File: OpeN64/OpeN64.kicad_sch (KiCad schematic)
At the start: 269 parts, among them P6 P5, SW1 N64_SW1_Power, SW2 RESET, U13 78M05, x1 Crystal_Small, x2 Crystal_Small

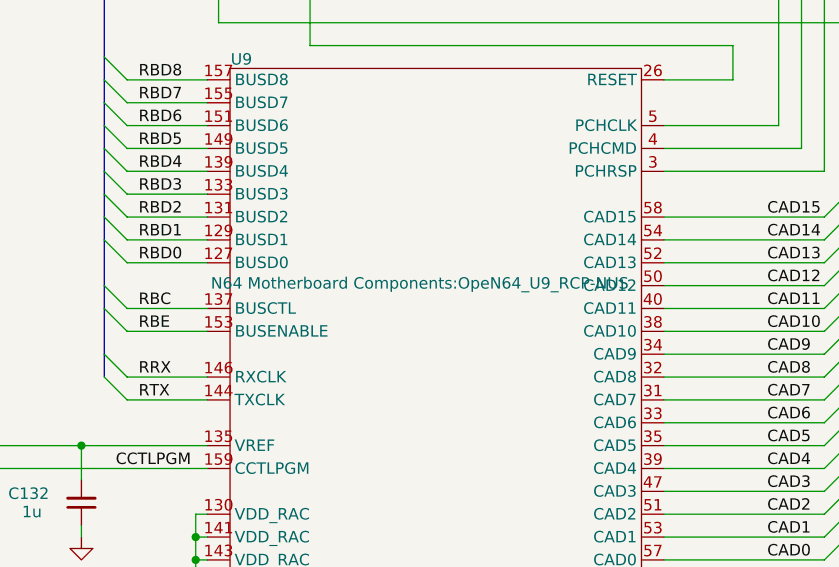
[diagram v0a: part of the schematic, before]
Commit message: Correct footprint associations after library rename
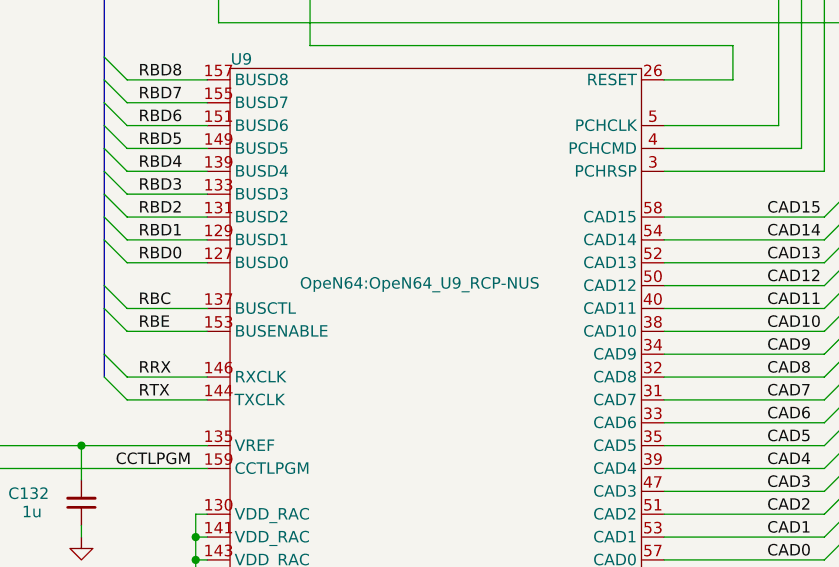
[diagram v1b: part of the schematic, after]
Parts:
- C1, C100, C101, C102, C103, C104, C105, C106, C107, C108, C109, C11, C110, C111, C113, C115, C116, C12, C120, C121, C122, C127, C129, C13, C136, C137, C139, C14, C143, C146, C147, C148, C150, C151, C152, C153, C154, C155, C156, C157, C158, C159, C160, C161, C162, C163, C164, C165, C166, C167, C168, C169, C17, C170, C172, C176, C177, C178, C179, C18, C19, C2, C20, C21, C22, C23, C27, C29, C3, C30, C31, C32, C35, C36, C38, C39, C4, C40, C41, C42, C45, C46, C47, C48, C49, C50, C51, C52, C54, C55, C56, C57, C58, C6, C64, C67, C68, C69, C7, C70, C71, C72, C75, C76, C77, C78, C8, C80, C83, C85, C86, C87, C88, C9, C90, C91, C93, C94, C96, C99, R1, R10, R11, R12, R13, R14, R15, R16, R17, R18, R19, R2, R20, R21, R22, R23, R28, R3, R31, R34, R36, R37, R38, R39, R4, R40, R5, R53, R54, R55, R56, R57, R58, R6, R7, R8, R9: footprint N64 Motherboard Components:OpeN64_SMD_0603 -> OpeN64:OpeN64_SMD_0603
- C10, C112, C114, C117, C118, C119, C123, C124, C125, C126, C132, C133, C135, C138, C144, C149, C37, C43, C44, C5, C53, C59, C60, C61, C62, C63, C65, C66, C74, C79, C82, C84, C89, C92, C95, C97, C98, R24, R25, R26, R27, R29, R30, R32, R33, R35: footprint N64 Motherboard Components:OpeN64_SMD_0805 -> OpeN64:OpeN64_SMD_0805
- C128, C34: footprint N64 Motherboard Components:OpeN64_CAP_AL_SMD_3.8x4.5 -> OpeN64:OpeN64_CAP_AL_SMD_3.8x4.5
- C130, C131, C134, C140, C141, C142, C145, C24, C28, C33, C73, C81: footprint N64 Motherboard Components:OpeN64_CAP_AL_SMD_6.2x4.7 -> OpeN64:OpeN64_CAP_AL_SMD_6.2x4.7
- C15, C16: footprint N64 Motherboard Components:OpeN64_CAP_AL_SMD_7.8x4.9 -> OpeN64:OpeN64_CAP_AL_SMD_7.8x4.9
- C173, C174, C175: footprint N64 Motherboard Components:OpeN64_SMD_1206 -> OpeN64:OpeN64_SMD_1206
- C25, C26: footprint N64 Motherboard Components:OpeN64_CAP_AL_SMD_3.8x4.5_Flipped -> OpeN64:OpeN64_CAP_AL_SMD_3.8x4.5_Flipped
- D1, D2: footprint N64 Motherboard Components:OpeN64_Diode -> OpeN64:OpeN64_Diode
- D3: footprint N64 Motherboard Components:OpeN64_D3_Red_LED -> OpeN64:OpeN64_D3_Red_LED
- D4, D5: footprint N64 Motherboard Components:OpeN64_Diode_Array_5_Pin -> OpeN64:OpeN64_Diode_Array_5_Pin
- DA1, DA3, DA5, DA6, DA7, DA8: footprint N64 Motherboard Components:OpeN64_Diode_Array -> OpeN64:OpeN64_Diode_Array
- FIL1, FIL2, FIL3, FIL4, FIL5, FIL6, FIL7, FIL8: footprint N64 Motherboard Components:OpeN64_Filter -> OpeN64:OpeN64_Filter
- P1: footprint N64 Motherboard Components:OpeN64_P1_RDRAM_Expansion_Port -> OpeN64:OpeN64_P1_RDRAM_Expansion_Port
- P2: footprint N64 Motherboard Components:OpeN64_P2_Left_Controller_Port -> OpeN64:OpeN64_P2_Left_Controller_Port
- P3: footprint N64 Motherboard Components:OpeN64_P3_Right_Controller_Port -> OpeN64:OpeN64_P3_Right_Controller_Port
- P4: footprint N64 Motherboard Components:OpeN64_P4_Power_Port -> OpeN64:OpeN64_P4_Power_Port
- P6: footprint N64 Motherboard Components:OpeN64_P5_Cartridge_Slot -> OpeN64:OpeN64_P5_Cartridge_Slot
- P7: footprint N64 Motherboard Components:OpeN64_P7_Video_Port -> OpeN64:OpeN64_P7_Video_Port
- Q1: footprint N64 Motherboard Components:OpeN64_Q_T23 -> OpeN64:OpeN64_Q_T23
- SW1: footprint N64 Motherboard Components:OpeN64_SW1_Power_Switch -> OpeN64:OpeN64_SW1_Power_Switch
- SW2: footprint N64 Motherboard Components:OpeN64_SW2_Reset -> OpeN64:OpeN64_SW2_Reset
- U1: footprint N64 Motherboard Components:OpeN64_U1_9480F -> OpeN64:OpeN64_U1_9480F
- U10: footprint N64 Motherboard Components:OpeN64_U10_CPU-NUS -> OpeN64:OpeN64_U10_CPU-NUS
- U11, U14: footprint N64 Motherboard Components:OpeN64_U11_14_RDRAM18-NUS -> OpeN64:OpeN64_U11_14_RDRAM18-NUS
- U12: footprint N64 Motherboard Components:OpeN64_U12_PQ7VZ5 -> OpeN64:OpeN64_U12_PQ7VZ5
- U13: footprint N64 Motherboard Components:OpeN64_U13_TO-252 -> OpeN64:OpeN64_U13_TO-252
- U15, U7: footprint N64 Motherboard Components:OpeN64_U7_15_MX8330 -> OpeN64:OpeN64_U7_15_MX8330
- U2: footprint N64 Motherboard Components:OpeN64_U2_AMP_NUS -> OpeN64:OpeN64_U2_AMP_NUS
- U3: footprint N64 Motherboard Components:OpeN64_U3_PST9128 -> OpeN64:OpeN64_U3_PST9128
- U4: footprint N64 Motherboard Components:OpeN64_U4_VDC-NUS -> OpeN64:OpeN64_U4_VDC-NUS
- U5: footprint N64 Motherboard Components:OpeN64_U5_ENC-NUS -> OpeN64:OpeN64_U5_ENC-NUS
- U6: footprint N64 Motherboard Components:OpeN64_U6_PIF -> OpeN64:OpeN64_U6_PIF
- U8: footprint N64 Motherboard Components:OpeN64_U8_LV125A -> OpeN64:OpeN64_U8_LV125A
- U9: footprint N64 Motherboard Components:OpeN64_U9_RCP-NUS -> OpeN64:OpeN64_U9_RCP-NUS
- x1, x2: footprint N64 Motherboard Components:OpeN64_CRYSTAL_HC49S_TH -> OpeN64:OpeN64_CRYSTAL_HC49S_TH

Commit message: Fixed embedded fonts
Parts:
- C172, C173, C174, C175, C176, C177, C178, C179, P1, P2, P3, P4, P7, Q1, U1, U10, U11, U12, U14, U15, U2, U3, U4, U5, U6, U7, U8, U9: value ~ -> (none)
